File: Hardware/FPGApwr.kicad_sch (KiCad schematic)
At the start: 20 parts, among them U3 XC7Z010-1CLG225I

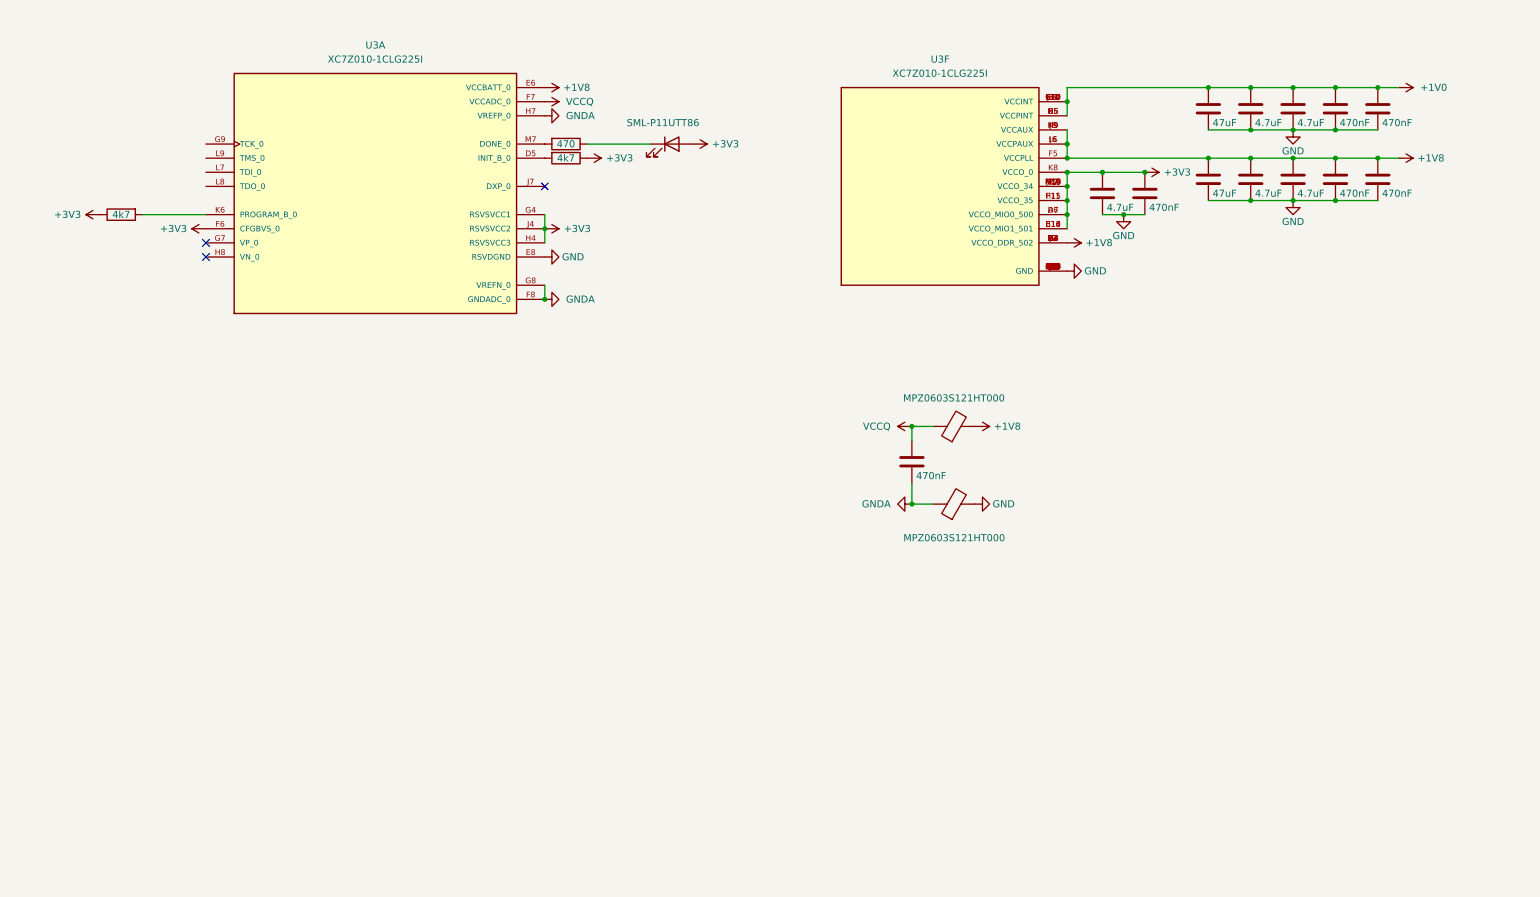
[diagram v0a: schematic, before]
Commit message: 11/19 update
add new header for jtag and fixed a couple of small things
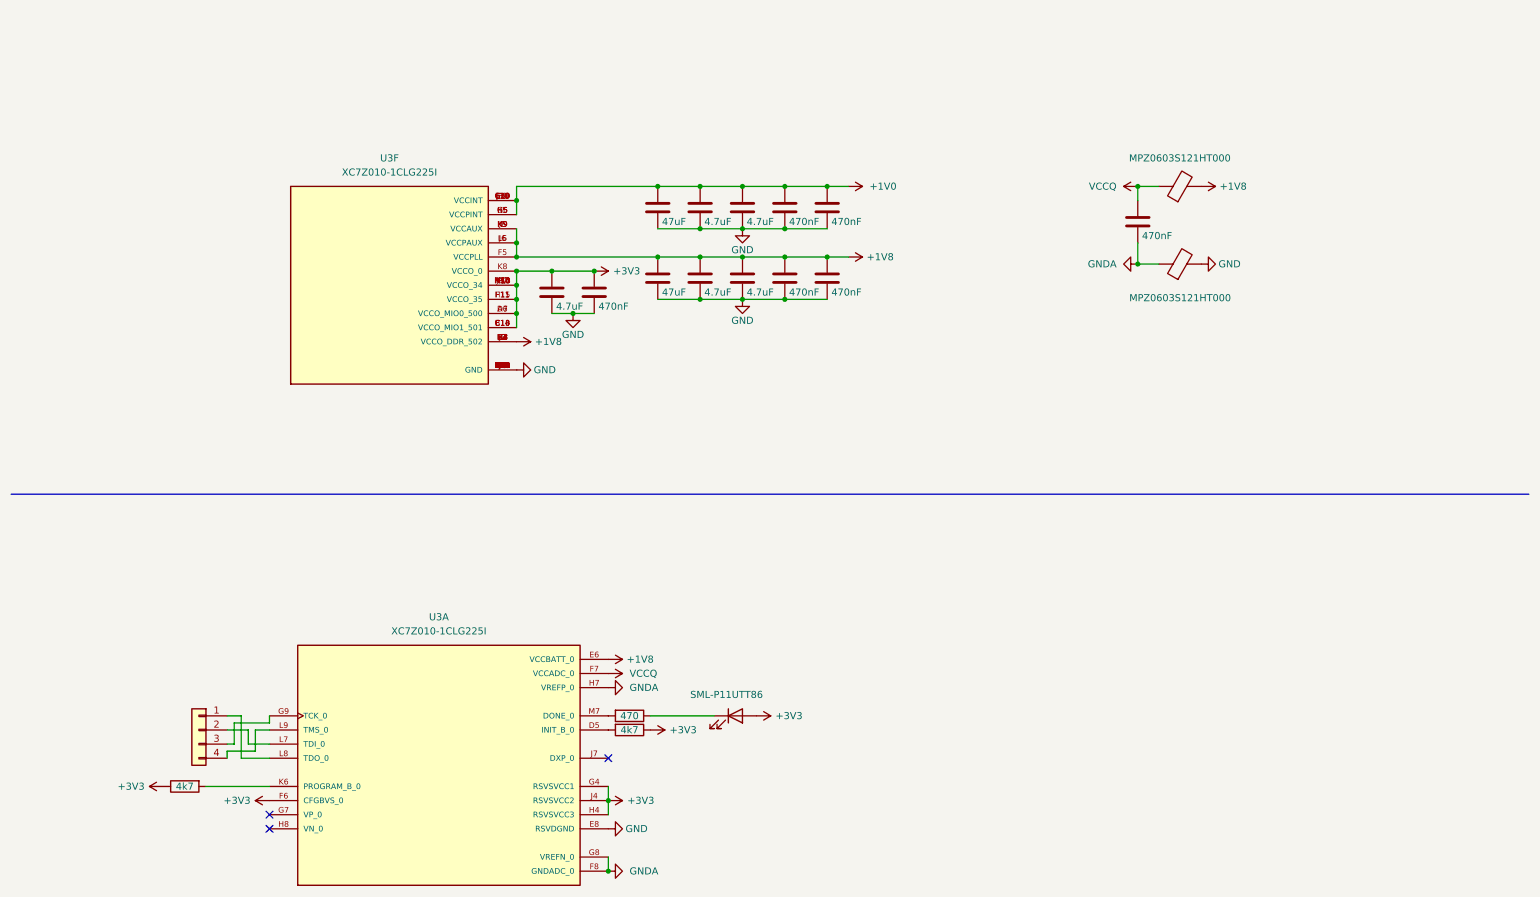
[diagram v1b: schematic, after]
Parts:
- added J7: Conn_01x04, Connector_PinHeader_1.27mm:PinHeader_2x02_P1.27mm_Vertical, symbol Connector_Generic:Conn_01x04
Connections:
- net at U3.G9 (TCK_0): now also J7.3 (Pin_3)
- net at U3.L7 (TDI_0): now also J7.2 (Pin_2)
- net at U3.L8 (TDO_0): now also J7.1 (Pin_1)
- net at U3.L9 (TMS_0): now also J7.4 (Pin_4)
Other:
- moved on the sheet: U3A, U3F

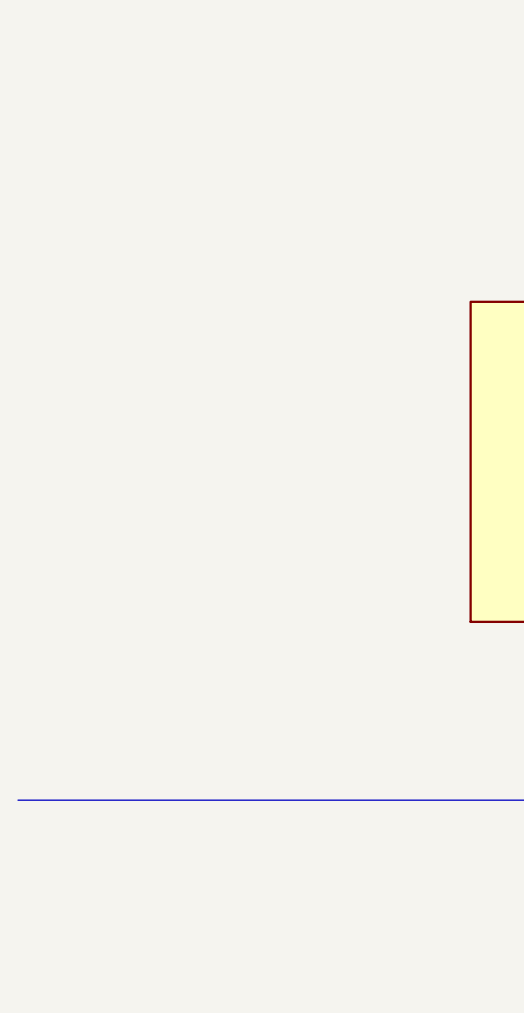
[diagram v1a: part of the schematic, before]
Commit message: 11/21 update
finished annotating the schematic and add pictures and output the pdf
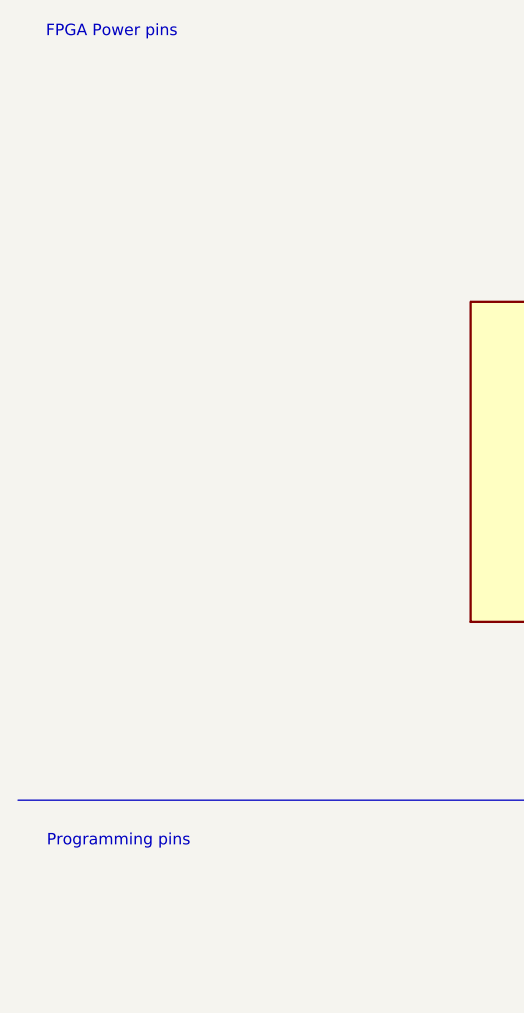
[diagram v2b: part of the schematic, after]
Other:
- note added: "FPGA Power pins"
- note added: "Programming pins"
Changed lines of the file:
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@@
+		)
+	)
+	(text "Programming pins"
+		(exclude_from_sim no)
+		(at 23.114 105.664 0)
+		(effects
+			(font
+				(size 1.27 1.27)
+			)
+		)
+	)
+	(text "FPGA Power pins"
+		(exclude_from_sim no)
+		(at 22.352 15.748 0)
+		(effects
+			(font
+				(size 1.27 1.27)
+			)
 		)
 	)
